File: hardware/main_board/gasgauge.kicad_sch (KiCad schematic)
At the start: 6 parts, among them U16 BQ27441DRZR-G1A

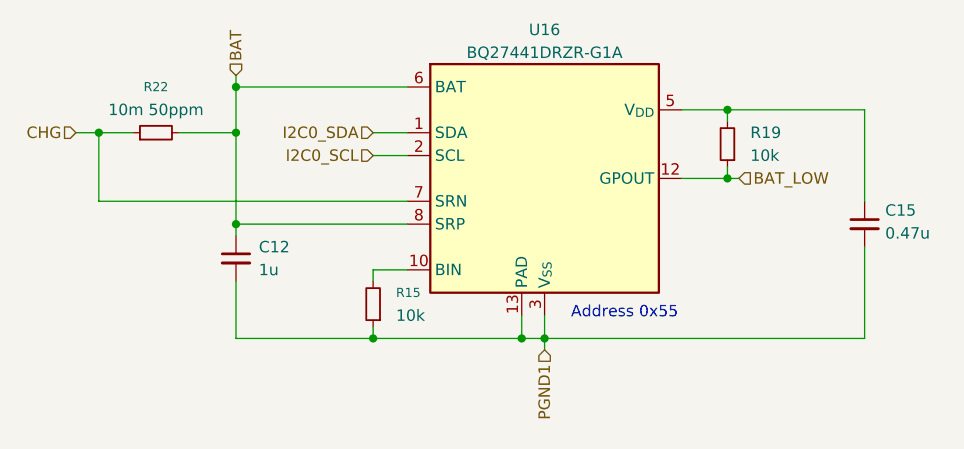
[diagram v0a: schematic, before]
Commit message: hardware(sch): update component package to 0402 as most as possable, layout is still need to complete
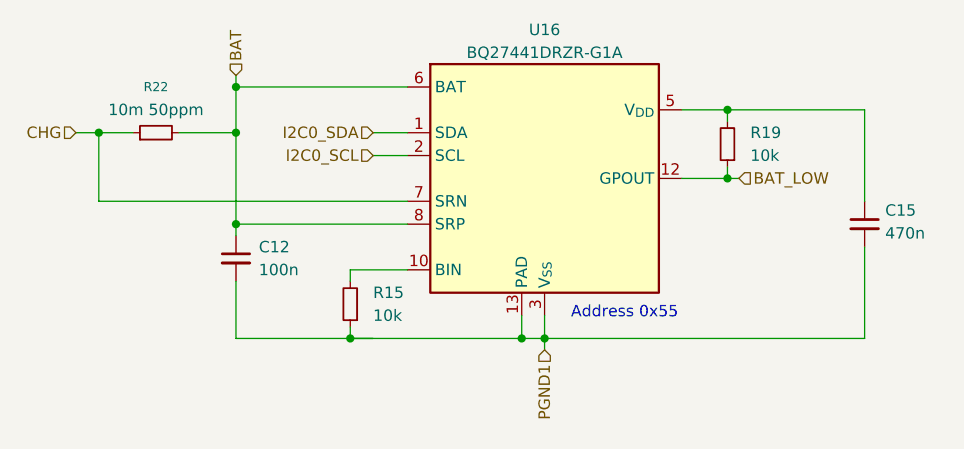
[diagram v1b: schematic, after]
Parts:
- C12: value 1u -> 100n; footprint Capacitor_SMD:C_0603_1608Metric -> Capacitor_SMD:C_0402_1005Metric; LCSC PN C5199872 -> C1525
- C15: value 0.47u -> 470n
- R15, R19: footprint Resistor_SMD:R_0603_1608Metric -> Resistor_SMD:R_0402_1005Metric; LCSC PN C98220 -> C25744
